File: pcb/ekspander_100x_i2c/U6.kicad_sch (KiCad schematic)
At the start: 4 parts, among them J15 DG127A-5.08-06P-14-00AH, J16 DG127A-5.08-06P-14-00AH, J17 DG127A-5.08-06P-14-00AH, U6 MCP23017_SP

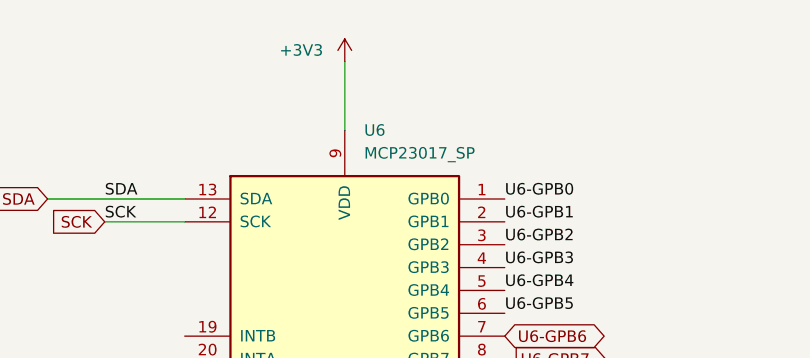
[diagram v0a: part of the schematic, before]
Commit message: Ekspander U2 - U3 - U4 update
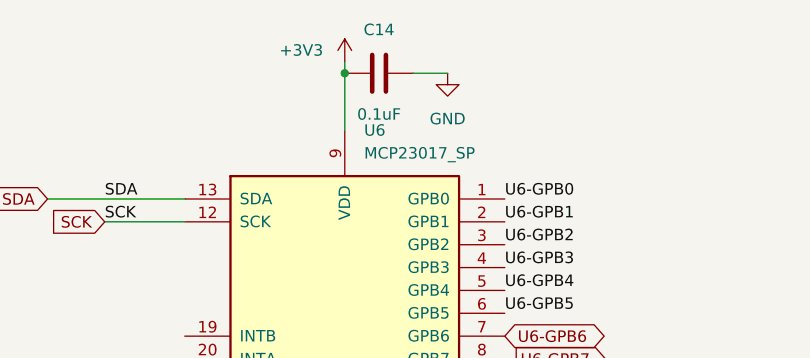
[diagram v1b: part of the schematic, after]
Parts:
- added C14: 0.1uF, Capacitor_SMD:C_0805_2012Metric_Pad1.18x1.45mm_HandSolder, symbol Device:C
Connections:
- net +3V3: now also C14.1
- net GND: now also C14.2
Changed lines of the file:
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@@
 	(generator_version "9.0")
 	(paper "A4")
+	(junction
+		(at 54.61 19.05)
+		(diameter 0)
+		(color 0 0 0 0)
+	)
 	(wire
 		(pts
@@
 	(wire
 		(pts
-			(xy 54.61 17.78) (xy 54.61 25.4)
+			(xy 54.61 17.78) (xy 54.61 19.05)
 		)
 		(stroke
@@
 		(pts
 			(xy 54.61 81.28) (xy 54.61 83.82)
+		)
+		(stroke
+			(width 0)
+			(type default)
+		)
+	)
+	(wire
+		(pts
+			(xy 66.04 19.05) (xy 62.23 19.05)
+		)
+		(stroke
+			(width 0)
+			(type default)
+		)
+	)
+	(wire
+		(pts
+			(xy 54.61 19.05) (xy 54.61 25.4)
 		)
 		(stroke
@@
 					(unit 1)
 				)
+			)
+		)
+	)
+	(symbol
+		(lib_id "Device:C")
+		(at 58.42 19.05 90)
+		(unit 1)
+		(exclude_from_sim no)
+		(in_bom yes)
+		(on_board yes)
+		(dnp no)
+		(property "Reference" "C14"
+			(at 58.42 14.224 90)
+			(effects
+				(font
+					(size 1.27 1.27)
+				)
+			)
+		)
+		(property "Value" "0.1uF"
+			(at 58.42 23.622 90)
+			(effects
+				(font
+					(size 1.27 1.27)
+				)
+			)
+		)
+		(property "Footprint" "Capacitor_SMD:C_0805_2012Metric_Pad1.18x1.45mm_HandSolder"
+			(at 62.23 18.0848 0)
+			(effects
+				(font
+					(size 1.27 1.27)
+				)
+				(hide yes)
+			)
+		)
+		(property "Datasheet" "~"
+			(at 58.42 19.05 0)
+			(effects
+				(font
+					(size 1.27 1.27)
+				)
+				(hide yes)
+			)
+		)
+		(property "Description" "Unpolarized capacitor"
+			(at 58.42 19.05 0)
+			(effects
+				(font
+					(size 1.27 1.27)
+				)
+				(hide yes)
+			)
+		)
+		(pin "2"
+		)
+		(pin "1"
+		)
+		(instances
+			(project "ekspander_100x_i2c"
+				(path "/824ceec5-564f-405b-8bea-e5a9f7aa2926/8bfbd7d0-83f8-4b04-af03-9d1fd88c9002"
+					(reference "C14")
+					(unit 1)
+				)
+			)
+		)
+	)
+	(symbol
+		(lib_id "power:GND")
+		(at 66.04 19.05 0)
+		(unit 1)
+		(exclude_from_sim no)
+		(in_bom yes)
+		(on_board yes)
+		(dnp no)
+		(fields_autoplaced yes)
+		(property "Reference" "#PWR041"
+			(at 66.04 25.4 0)
+			(effects
+				(font
+					(size 1.27 1.27)
+				)
+				(hide yes)
+			)
+		)
+		(property "Value" "GND"
+			(at 66.04 24.13 0)
+			(effects
+				(font
+					(size 1.27 1.27)
+				)
+			)
+		)
+		(property "Footprint" ""
+			(at 66.04 19.05 0)
+			(effects
+				(font
+					(size 1.27 1.27)
+				)
+				(hide yes)
+			)
+		)
+		(property "Datasheet" ""
+			(at 66.04 19.05 0)
+			(effects
+				(font
+					(size 1.27 1.27)
+				)
+				(hide yes)
+			)
+		)
+		(property "Description" "Power symbol creates a global label with name \"GND\" , ground"
+			(at 66.04 19.05 0)
+			(effects
+				(font
+					(size 1.27 1.27)
+				)
+				(hide yes)
+			)
+		)
+		(pin "1"
+		)
+		(instances
+			(project "ekspander_100x_i2c"
+				(path "/824ceec5-564f-405b-8bea-e5a9f7aa2926/8bfbd7d0-83f8-4b04-af03-9d1fd88c9002"
+					(reference "#PWR041")
+					(unit 1)
+				)

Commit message: Ekspander U5 - U6 update
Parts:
- added C25, C26: 0.1uF, Capacitor_SMD:C_0805_2012Metric_Pad1.18x1.45mm_HandSolder, symbol Device:C
- added U30, U33: LTV-847, Package_DIP:DIP-16_W7.62mm, symbol Isolator:LTV-847
- added U31, U32: ITS716G, Package_SO:SOIC-20W_7.5x12.8mm_P1.27mm, symbol Driver_FET:ITS716G
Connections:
- net GND: now also C25.2, C26.2, U30.11, U30.13, U30.15, U30.2, U30.4, U30.6, U30.8, U30.9, U31.2 (GND1/2), U31.6 (GND3/4), U32.2 (GND1/2), U32.6 (GND3/4), U33.11, U33.13, U33.15, U33.2, U33.4, U33.6, U33.8, U33.9
- net U6-GPA0: now also U33.10
- net U6-GPA1: now also U33.12
- net U6-GPA2: now also U33.14
- net U6-GPA3: now also U33.16
- net U6-GPA4: now also U32.9 (IN4)
- net U6-GPA5: now also U32.7 (IN3)
- net U6-GPA6: now also U32.5 (IN2)
- net U6-GPA7: now also U32.3 (IN1)
- net U6-GPB0: now also U30.16
- net U6-GPB1: now also U30.14
- net U6-GPB2: now also U30.12
- net U6-GPB3: now also U30.10
- net U6-GPB4: now also U31.3 (IN1)
- net U6-GPB5: now also U31.5 (IN2)
- net U6-GPB6: now also U31.7 (IN3)
- net U6-GPB7: now also U31.9 (IN4)
- net ZC79_CLOSE_LED: now reaches J16.1
- net ZC79_CLOSE_LED: now also U33.3
- net ZC79_OPEN_LED: now reaches J16.2
- net ZC79_OPEN_LED: now also U33.1
- net ZC78_CLOSE_MOTOR: now reaches J16.3
- net ZC78_CLOSE_MOTOR: now also U31.13 (OUT4)
- net ZC78_OPEN_MOTOR: now reaches J16.4
- net ZC78_OPEN_MOTOR: now also U31.14 (OUT3)
- net ZC77_CLOSE_MOTOR: now reaches J16.5
- net ZC77_CLOSE_MOTOR: now also U31.17 (OUT2)
- net ZC77_OPEN_MOTOR: now reaches J16.6
- net ZC77_OPEN_MOTOR: now also U31.18 (OUT1)
- net ZC78_CLOSE_LED: now reaches J15.1
- net ZC78_CLOSE_LED: now also U30.5
- net ZC78_OPEN_LED: now reaches J15.2
- net ZC78_OPEN_LED: now also U30.7
- net ZC77_CLOSE_LED: now reaches J15.3
- net ZC77_CLOSE_LED: now also U30.3
- net ZC77_OPEN_LED: now reaches J15.4
- net ZC77_OPEN_LED: now also U30.1
- net ZC76_CLOSE_MOTOR: now reaches J15.5
- net ZC76_OPEN_MOTOR: now reaches J15.6
- net ZC80_CLOSE_MOTOR: now reaches J17.1
- net ZC80_CLOSE_MOTOR: now also U32.13 (OUT4)
- net ZC80_OPEN_MOTOR: now reaches J17.2
- net ZC80_OPEN_MOTOR: now also U32.14 (OUT3)
- net ZC79_CLOSE_MOTOR: now reaches J17.3
- net ZC79_CLOSE_MOTOR: now also U32.17 (OUT2)
- net ZC79_OPEN_MOTOR: now reaches J17.4
- net ZC79_OPEN_MOTOR: now also U32.18 (OUT1)
- net ZC80_OPEN_LED: now reaches J17.5
- net ZC80_OPEN_LED: now also U33.7
- net ZC80_CLOSE_LED: now reaches J17.6
- net ZC80_CLOSE_LED: now also U33.5
- new net +24V: C25.1, C26.1, U31.1 (VBB), U31.10 (VBB), U31.11 (VBB), U31.12 (VBB), U31.15 (VBB), U31.16 (VBB), U31.19 (VBB), U31.20 (VBB), U32.1 (VBB), U32.10 (VBB), U32.11 (VBB), U32.12 (VBB), U32.15 (VBB), U32.16 (VBB), U32.19 (VBB), U32.20 (VBB)
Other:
- moved on the sheet: J15, J16, J17

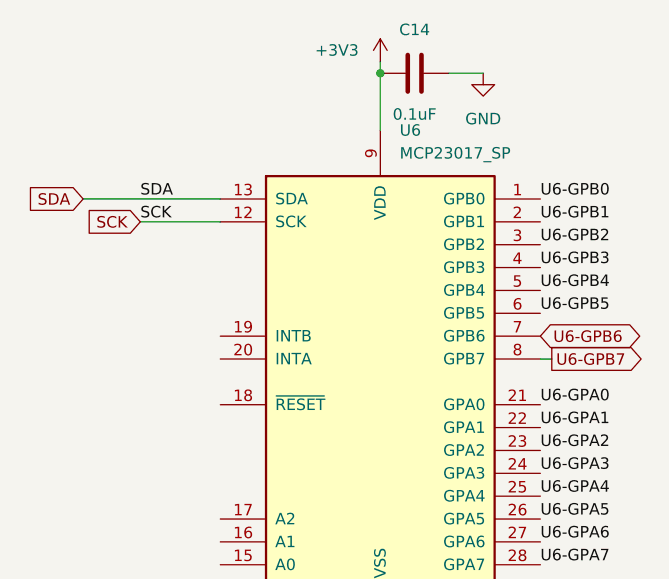
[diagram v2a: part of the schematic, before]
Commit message: Ekspander 24V update
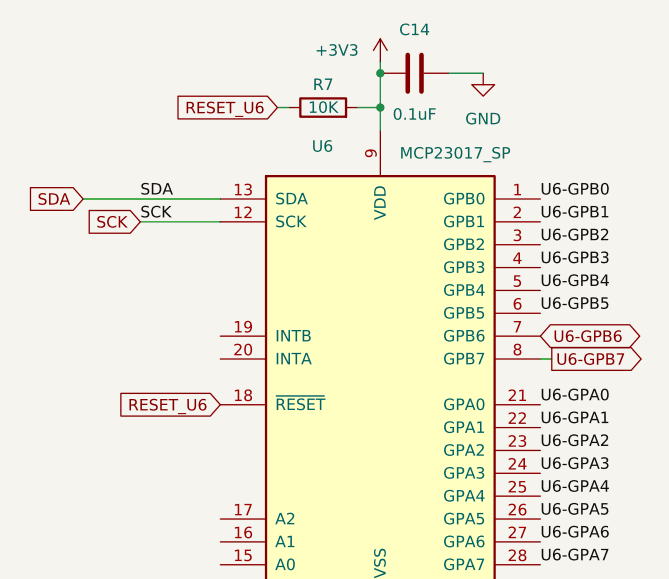
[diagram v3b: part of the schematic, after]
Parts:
- added R7: 10K, PCM_Resistor_SMD_AKL:R_0805_2012Metric_Pad1.20x1.40mm_HandSolder, symbol Device:R
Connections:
- net +3V3: now also R7.2
- net RESET_U6: now reaches U6.18 (~{RESET})
- net RESET_U6: now also R7.1
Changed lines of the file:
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@@
 	)
 	(junction
+		(at 54.61 22.86)
+		(diameter 0)
+		(color 0 0 0 0)
+	)
+	(junction
 		(at 200.66 149.86)
 		(diameter 0)
@@
 	(wire
 		(pts
+			(xy 43.18 22.86) (xy 44.45 22.86)
+		)
+		(stroke
+			(width 0)
+			(type default)
+		)
+	)
+	(wire
+		(pts
 			(xy 200.66 134.62) (xy 200.66 149.86)
 		)
@@
 	(wire
 		(pts
+			(xy 54.61 22.86) (xy 54.61 25.4)
+		)
+		(stroke
+			(width 0)
+			(type default)
+		)
+	)
+	(wire
+		(pts
 			(xy 180.34 104.14) (xy 180.34 119.38)
 		)
@@
 	(wire
 		(pts
+			(xy 52.07 22.86) (xy 54.61 22.86)
+		)
+		(stroke
+			(width 0)
+			(type default)
+		)
+	)
+	(wire
+		(pts
 			(xy 227.33 30.48) (xy 227.33 52.07)
 		)
@@
 	(wire
 		(pts
-			(xy 54.61 19.05) (xy 54.61 25.4)
+			(xy 54.61 19.05) (xy 54.61 22.86)
 		)
 		(stroke
@@
 		)
 	)
+	(global_label "RESET_U6"
+		(shape input)
+		(at 43.18 22.86 180)
+		(fields_autoplaced yes)
+		(effects
+			(font
+				(size 1.27 1.27)
+			)
+			(justify right)
+		)
+		(property "Intersheetrefs" "${INTERSHEET_REFS}"
+			(at 30.9421 22.86 0)
+			(effects
+				(font
+					(size 1.27 1.27)
+				)
+				(justify right)
+				(hide yes)
+			)
+		)
+	)
 	(global_label "U6-GPB6"
 		(shape bidirectional)
@@
 		)
 	)
+	(global_label "RESET_U6"
+		(shape input)
+		(at 36.83 55.88 180)
+		(fields_autoplaced yes)
+		(effects
+			(font
+				(size 1.27 1.27)
+			)
+			(justify right)
+		)
+		(property "Intersheetrefs" "${INTERSHEET_REFS}"
+			(at 24.5921 55.88 0)
+			(effects
+				(font
+					(size 1.27 1.27)
+				)
+				(justify right)
+				(hide yes)
+			)
+		)
+	)
 	(global_label "ZC78_OPEN_LED"
 		(shape input)
@@
 		(on_board yes)
 		(dnp no)
-		(fields_autoplaced yes)
 		(property "Reference" "U6"
-			(at 56.7533 25.4 0)
+			(at 46.99 27.178 0)
 			(effects
 				(font
@@
 					(unit 1)
 				)
+			)
+		)
+	)
+	(symbol
+		(lib_id "Device:R")
+		(at 48.26 22.86 90)
+		(unit 1)
+		(exclude_from_sim no)
+		(in_bom yes)
+		(on_board yes)
+		(dnp no)
+		(property "Reference" "R7"
+			(at 48.26 20.32 90)
+			(effects
+				(font
+					(size 1.27 1.27)
+				)
+			)
+		)
+		(property "Value" "10K"
+			(at 48.26 22.86 90)
+			(effects
+				(font
+					(size 1.27 1.27)
+				)
+			)
+		)
+		(property "Footprint" "PCM_Resistor_SMD_AKL:R_0805_2012Metric_Pad1.20x1.40mm_HandSolder"
+			(at 48.26 24.638 90)
+			(effects
+				(font
+					(size 1.27 1.27)
+				)
+				(hide yes)
+			)
+		)
+		(property "Datasheet" "~"
+			(at 48.26 22.86 0)
+			(effects
+				(font
+					(size 1.27 1.27)
+				)
+				(hide yes)
+			)
+		)
+		(property "Description" "Resistor"
+			(at 48.26 22.86 0)
+			(effects
+				(font
+					(size 1.27 1.27)
+				)
+				(hide yes)
+			)
+		)
+		(pin "2"
+		)
+		(pin "1"
+		)
+		(instances
+			(project "ekspander_100x_i2c"
+				(path "/824ceec5-564f-405b-8bea-e5a9f7aa2926/8bfbd7d0-83f8-4b04-af03-9d1fd88c9002"
+					(reference "R7")
+					(unit 1)
+				)
